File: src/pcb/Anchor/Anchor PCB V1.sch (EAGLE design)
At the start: 8 parts, among them Q1 48 MHz, U1 ATSAMD21G-A

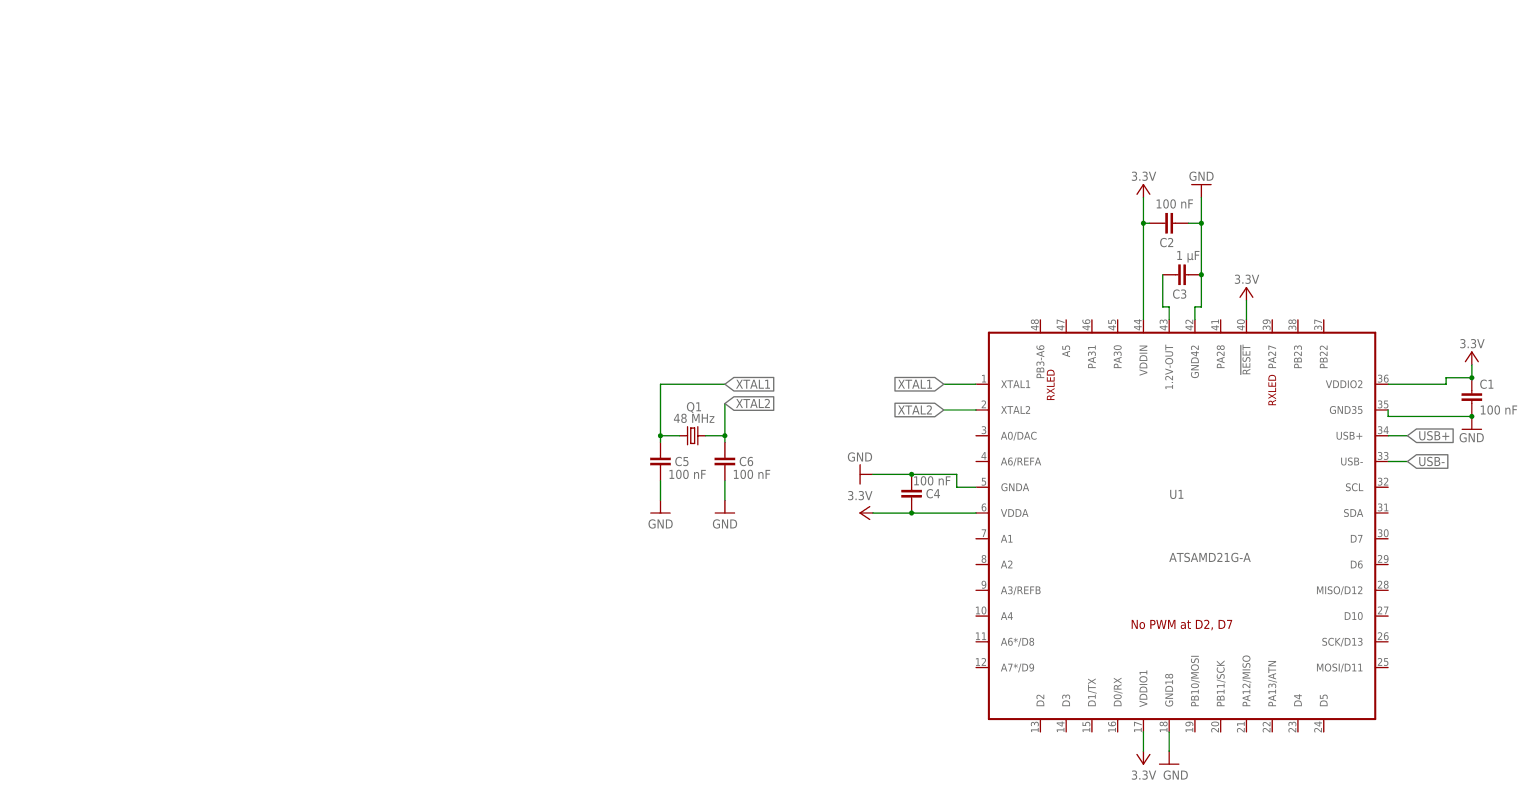
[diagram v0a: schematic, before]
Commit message: Added components
Added DC DC converter
Added reset button
Added mini-USB connection
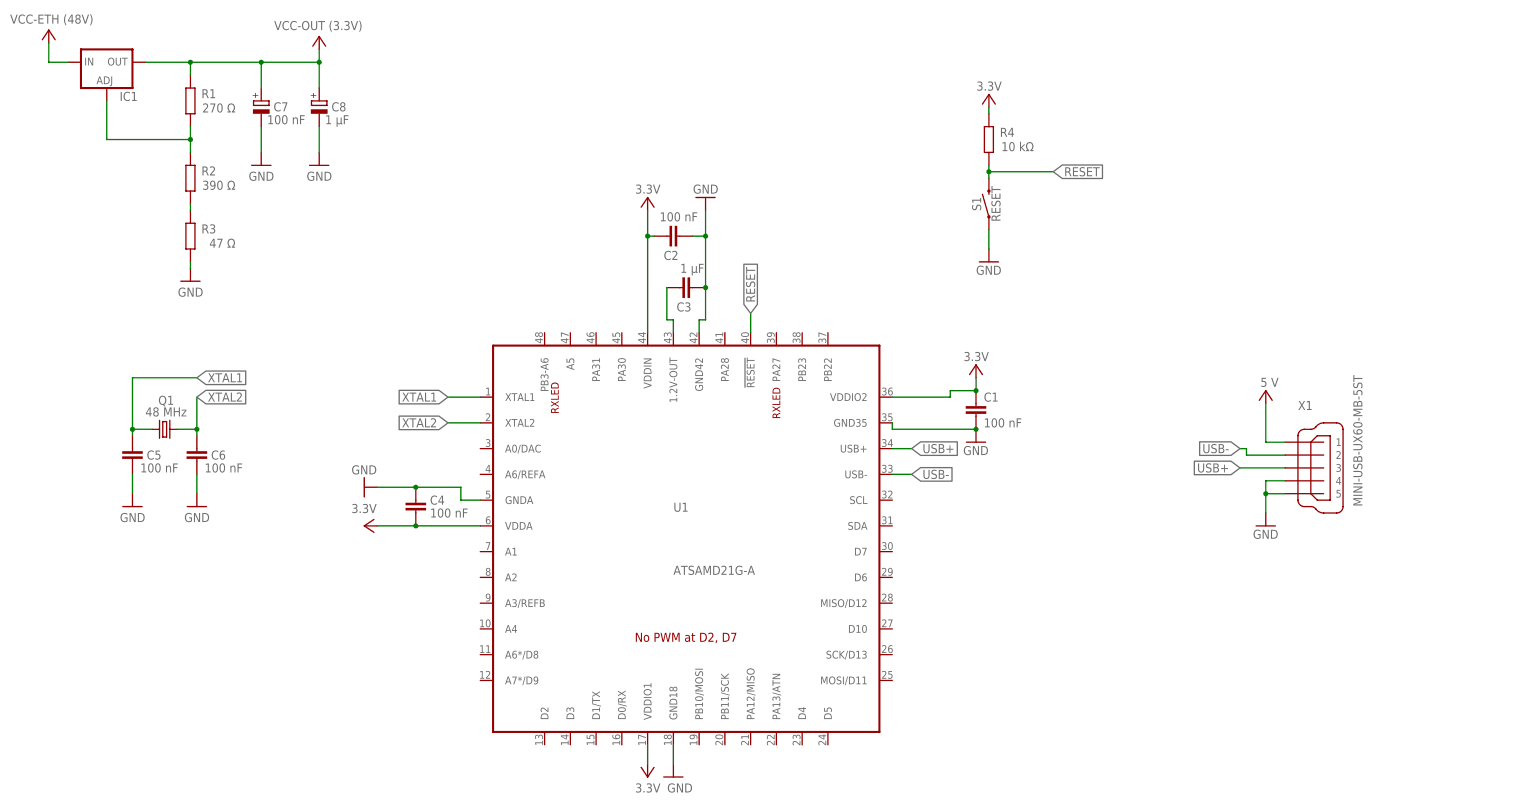
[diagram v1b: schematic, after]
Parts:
- added C7: 100 nF, rcl:CPOL-EUE7.5-18
- added C8: 1 µF, rcl:CPOL-EUE7.5-18
- added IC1: (no value), v-reg:LM317TL
- added R1: 270 Ω, rcl:R-EU_M0805
- added R2: 390 Ω, rcl:R-EU_M0805
- added R3: 47 Ω, rcl:R-EU_M0805
- added R4: 10 kΩ, rcl:R-EU_M0805
- added S1: RESET, SparkFun-Switches:MOMENTARY-SWITCH-SPST-PTH-6.0MM-KIT
- added X1: MINI-USB-UX60-MB-5ST, con-hirose:MINI-USB-UX60-MB-5ST
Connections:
- new net N$4: IC1.ADJ, R1.1, R2.2
- new net N$5: X1.3
- new net N$6: R2.1, R3.2
- new net N$7: X1.2
- new net N$8: R4.1, S1.2
- new net RESET: U1.!RESET!
- net GND: now also C7.-, C8.-, R3.1, S1.1, X1.4, X1.5
- net VCC: now also C7.+, C8.+, IC1.IN, IC1.OUT, R1.2, R4.2, X1.1; no longer U1.!RESET!
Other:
- moved on the sheet: C1, C2, C3, C4, C5, C6, Q1, U1

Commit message: Completed schematic anchor with PoE
PCB design has not been done yet.
Changes might happen in the future
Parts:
- added 10-PIN-PROGRAMMER: (no value), con-lsta:FE05-2
- added BR1, BR2: HD04-T, HD04-T:HD04-T
- added C10: 560 pF, rcl:C-EUC0805
- added C11: 15 pF, rcl:C-EUC0805
- added C12: 33 nF, rcl:C-EUC0805
- added C13: 47 µF (63V), rcl:CPOL-EUB45181D
- added C14, C15: 1 µF (100V), rcl:C-EUC0805
- added C16: 1 µF (16V), rcl:C-EUC0805
- added C17: 0.22 µF (10V), rcl:C-EUC0805
- added C18: 0.1 µF, rcl:C-EUC0805
- added C19, C20, C21: 10 µF (6.3V), rcl:C-EUC0805
- added C22, C24: 10 µF, rcl:CPOL-EUE5-5
- added C23: 100 µF (6.3V), rcl:CPOL-EUUD-5X5,8
- added C25, C26: 100 nF, rcl:C-EUC0805
- added C27: 10 µF, rcl:C-EUC0805
- added C28, C29: 18 µF, rcl:C-EUC0805
- added C9: 0.1 µF (100V), rcl:C-EUC0805
- added D1: SMAJ58A, SMAJ58A:SMAJ58A
- added D2: 6CWQ10FN, shottky:BAS70-05DPAK
- added D3: POWER, SparkFun-LED:LED-BLUE1206
- added D4, D6: TX, SparkFun-LED:LED-YELLOWLILYPAD
- added D5, D7: RX, SparkFun-LED:LED-GREENLILYPAD
- added IC2: TPS23750PWP, TPS23750PWP:TPS23750PWP
- added IC3: REG1117, burr-brown:REG1117
- added IC4: DWM1000, DWM1000:DWM1000
- added J1: 0826-1X1T-GJ-F, 0826-1X1T-GJ-F:0826-1X1T-GJ-F
- added JP1: (no value), jumper:JP1E
- added L1: FB_1206, rc-master-smd:FB_1206
- added L1(74437336100): 10 µH, inductors:DR73
- added L2: 33 µH, inductors:DR73
- added Q2: SUD06N10-225L, transistor-power:N-HEXFET_SOT323-IRLL014N
- added R10: 10 Ω, rcl:R-EU_R0805
- added R11: 1.5 kΩ, rcl:R-EU_R0805
- added R12: 3.48 kΩ, rcl:R-EU_R0805
- added R13: 51.1 Ω, rcl:R-EU_R0805
- added R14, R28: 270 Ω, rcl:R-EU_R0805
- added R15, R16, R17, R18: 49.9 Ω, rcl:R-EU_R0805
- added R19: 2.32 kΩ 1%, rcl:R-EU_R0805
- added R20, R21, R22: 330 Ω, rcl:R-EU_R0805
- added R23: 1 kΩ, rcl:R-EU_R0805
- added R24, R25: 100 Ω, rcl:R-EU_R0805
- added R26, R29: 220 Ω, rcl:R-EU_R0805
- added R27: 10 kΩ, rcl:R-EU_M0805
- added R5: 24,9 kΩ, rcl:R-EU_R0805
- added R6: 100 kΩ, rcl:R-EU_R0805
- added R7: 357 Ω (0.25W), rcl:R-EU_R0805
- added R8: 75 kΩ, rcl:R-EU_R0805
- added R9: 0.18 mΩ (0.5W), rcl:R-EU_R0805
- added Y1: 25 MHz, SparkFun-Clocks:CRYSTALSMD-HC49UP
- C7: device rcl:CPOL-EUE7.5-18 -> rcl:CPOL-EUE5-5
- C8: device rcl:CPOL-EUE7.5-18 -> rcl:CPOL-EUE5-4
- IC1: value (none) -> ENC28J60-I_SS; device v-reg:LM317TL -> ENC28J60-I_SS:ENC28J60-I_SS
- R2: value 390 Ω -> 443 Ω
- R3: value 47 Ω -> 470 Ω; device rcl:R-EU_M0805 -> rcl:R-EU_R0805
- S1: device SparkFun-Switches:MOMENTARY-SWITCH-SPST-PTH-6.0MM-KIT -> SparkFun-Switches:MOMENTARY-SWITCH-SPST-SMD-4.5MM
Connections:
- new net 1_VC+: BR1.~_2, J1.VC12
- new net 1_VC-: BR1.~_1, J1.VC36
- new net 2_VC+: BR2.~_2, J1.VC45
- new net 2_VC-: BR2.~_1, J1.VC78
- new net AUX: C16.1, IC2.AUX
- new net COMP: C11.2, IC2.COMP, R6.2
- new net COM_A_SHTKY: D2.A1, D2.A2, L2.1, Q2.D
- new net CS1: IC1.~CS
- new net CSN_DWM: IC4.SPICSN, U1.D10
- new net FB: C10.1, C11.1, IC2.FB
- new net FREQ: IC2.FREQ, R8.2
- new net GATE: IC2.GATE, R10.1
- new net GRN_CAT: J1.GRN_CAT, R24.1
- new net GRN_LED: IC1.LEDA, J1.GRN_AN
- new net IRQ: IC4.IRQ/GPIO8, R27.2
- new net MISO1_MC: R20.1, U1.PA12/MISO
- new net MISO2_MC: IC4.SPIMISO, U1.MISO/D12
- new net MOSI1_MC: R21.1, U1.PB10/MOSI
- new net MOSI2_MC: IC4.SPIMOSI, U1.MOSI/D11
- new net N$10: R12.1, R13.2
- new net N$11: D4.A, R14.1
- new net N$12: D5.A, R26.1
- new net N$13: D6.A, R28.1
- new net N$14: D7.A, R29.1
- new net N$9: D3.A, R3.1
- new net OSC1: C28.1, IC1.OSC1, Y1.1
- new net OSC2: C29.1, IC1.OSC2, Y1.2
- new net POE+: BR1.+, BR2.+, C13.+, C9.1, D1.K, IC2.VDD, L1(74437336100).1, R5.2
- new net REG_GND: C22.+, IC3.GND, R1.1, R2.2
- new net RSP: IC2.RSP, Q2.S, R9.2
- new net RST_DWM: IC4.RSTN, U1.D6
- new net RTN: C12.2, C13.-, C14.2, C15.2, C16.2, C17.2, IC2.BL, IC2.COM, IC2.MODE, IC2.RSN, IC2.RTN, R8.1, R9.1
- new net RXLED_DWM: D7.C, IC4.GPIO2_/_RXLED
- new net RX_MC: D5.C, U1.D0/RX, U1.PB23
- new net SCK1_MC: R22.1, U1.PB11/SCK
- new net SCK2_MC: IC4.SPICLK, U1.SCK/D13
- new net SCK_ETH: IC1.SCK, R22.2
- new net SEN: C18.1, IC2.SEN, R11.1, R12.2
- new net SI_ETH: IC1.SI, R21.2
- new net SO_ETH: IC1.SO, R20.2
- new net SWCLK: 10-PIN-PROGRAMMER.4, R23.1, U1.PA30
- new net SWDIO: 10-PIN-PROGRAMMER.2, U1.PA31
- new net SWO: 10-PIN-PROGRAMMER.6
- new net TMR: C12.1, IC2.TMR
- new net TPIN+: IC1.TPIN+, J1.TRD2+, R17.1
- new net TPIN-: IC1.TPIN-, J1.TRD2-, R18.2
- new net TPOUT+: IC1.TPOUT+, J1.TRD1+, R15.1
- new net TPOUT-: IC1.TPOUT-, J1.TRD1-, R16.2
- new net TXLED_DWM: D6.C, IC4.GPIO3_/_TXLED
- new net TX_MC: D4.C, U1.D1/TX, U1.PB22
- new net VBIAS: C17.1, IC2.VBIAS
- new net VBUS: X1.1
- new net VCAP: C27.1, IC1.VCAP
- new net VOUT+: C14.1, C15.1, C19.1, C20.1, C21.1, C23.+, C24.+, D2.C, IC2.SENP, IC3.VIN, JP1.1, L1(74437336100).2, R11.2
- new net YEL_CAT: J1.YEL_CAT, R25.1
- new net YEL_LED: IC1.LEDB, J1.YEL_AN
- net GND: now also 10-PIN-PROGRAMMER.3, 10-PIN-PROGRAMMER.5, 10-PIN-PROGRAMMER.9, BR1.-, BR2.-, C18.2, C19.2, C20.2, C21.2, C22.-, C23.-, C24.-, C25.2, C26.2, C27.2, C28.2, C29.2, C9.2, D1.A, D3.C, IC1.VSS, IC1.VSSOSC, IC1.VSSPLL, IC1.VSSRX, IC1.VSSTX, IC2.POWERPAD, IC2.VSS, IC4.VSS_1, IC4.VSS_2, IC4.VSS_3, IC4.VSS_4, IC4.VSS_5, JP1.2, L2.2, R13.1, R19.2, R2.1, R24.2, R25.2, R27.1, R7.1; no longer R3.1
- net N$2: now also IC2.DET, R5.1; no longer C5.1, Q1.2
- net N$3: now also IC2.CLASS, R7.2; no longer C6.1, Q1.1
- net N$4: now also C25.1, J1.TRCT1, L1.1, R15.2, R16.1; no longer IC1.ADJ, R1.1, R2.2
- net N$5: now also C10.2, R6.1; no longer X1.3
- net N$6: now also C26.1, J1.TRCT2, R17.2, R18.1; no longer R2.1, R3.2
- net N$7: now also Q2.G, R10.2; no longer X1.2
- net N$8: now also IC1.RBIAS, R19.1; no longer R4.1, S1.2
- net RESET: now also 10-PIN-PROGRAMMER.10, R4.1, S1.2
- net USB+: now also X1.3
- net USB-: now also X1.2
- net VCC: now also 10-PIN-PROGRAMMER.1, IC1.VDD, IC1.VDDOSC, IC1.VDDPLL, IC1.VDDRX, IC1.VDDTX, IC1.~RESET, IC3.VOUT, IC4.VDD3V3_1, IC4.VDDAON, L1.2, R14.2, R23.2, R26.2, R28.2, R29.2, R3.2; no longer IC1.IN, IC1.OUT, X1.1
- net XTAL1: now also C5.1, Q1.2
- net XTAL2: now also C6.1, Q1.1
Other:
- moved on the sheet: C1, C2, C3, C4, C5, C6, C7, C8, Q1, R1, R2, R3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

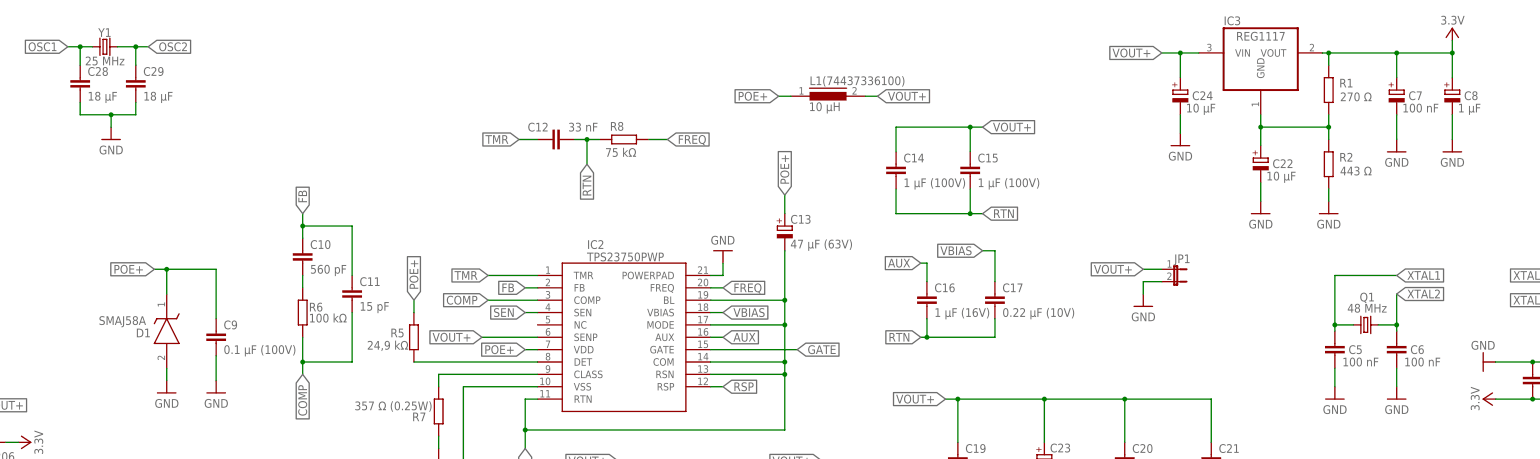
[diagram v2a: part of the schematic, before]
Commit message: Updated capacitor values XTAL
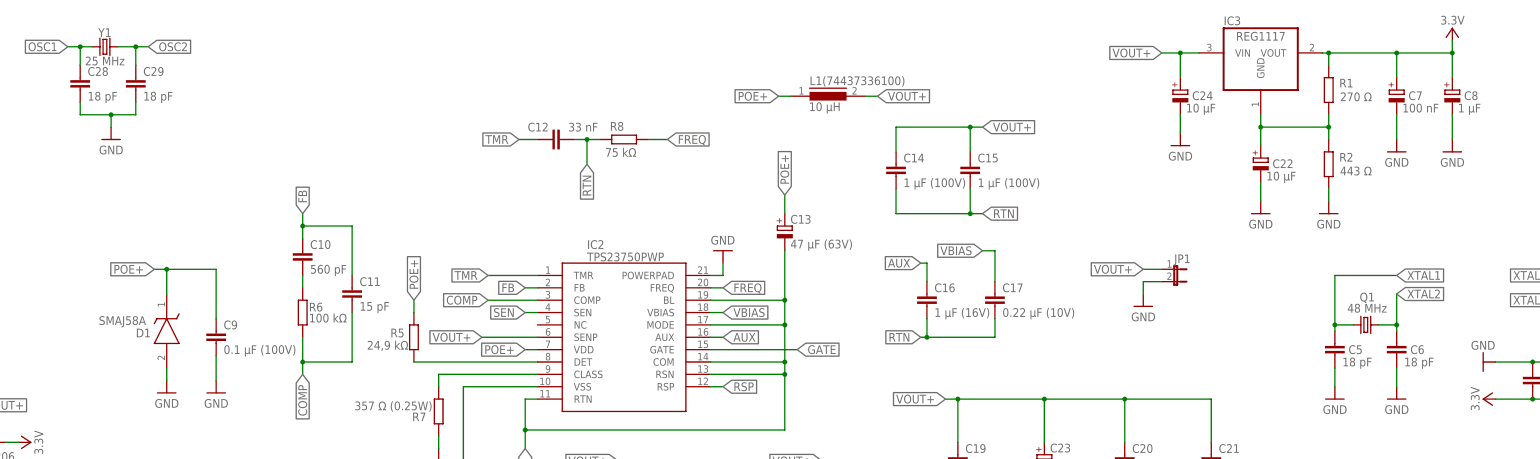
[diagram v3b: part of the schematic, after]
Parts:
- C28, C29: value 18 µF -> 18 pF
- C5, C6: value 100 nF -> 18 pF
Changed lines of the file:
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@@
 <part name="C4" library="rcl" library_urn="urn:adsk.eagle:library:334" deviceset="C-EU" device="C0805" package3d_urn="urn:adsk.eagle:package:23617/2" value="100 nF"/>
 <part name="GND4" library="supply1" library_urn="urn:adsk.eagle:library:371" deviceset="GND" device=""/>
-<part name="C5" library="rcl" library_urn="urn:adsk.eagle:library:334" deviceset="C-EU" device="C0805" package3d_urn="urn:adsk.eagle:package:23617/2" value="100 nF"/>
-<part name="C6" library="rcl" library_urn="urn:adsk.eagle:library:334" deviceset="C-EU" device="C0805" package3d_urn="urn:adsk.eagle:package:23617/2" value="100 nF"/>
+<part name="C5" library="rcl" library_urn="urn:adsk.eagle:library:334" deviceset="C-EU" device="C0805" package3d_urn="urn:adsk.eagle:package:23617/2" value="18 pF"/>
+<part name="C6" library="rcl" library_urn="urn:adsk.eagle:library:334" deviceset="C-EU" device="C0805" package3d_urn="urn:adsk.eagle:package:23617/2" value="18 pF"/>
 <part name="GND5" library="supply1" library_urn="urn:adsk.eagle:library:371" deviceset="GND" device=""/>
 <part name="GND6" library="supply1" library_urn="urn:adsk.eagle:library:371" deviceset="GND" device=""/>
@@
 <part name="P+11" library="supply1" library_urn="urn:adsk.eagle:library:371" deviceset="VCC" device="" value="3.3V"/>
 <part name="GND40" library="supply1" library_urn="urn:adsk.eagle:library:371" deviceset="GND" device=""/>
-<part name="C28" library="rcl" library_urn="urn:adsk.eagle:library:334" deviceset="C-EU" device="C0805" package3d_urn="urn:adsk.eagle:package:23617/2" value="18 µF"/>
-<part name="C29" library="rcl" library_urn="urn:adsk.eagle:library:334" deviceset="C-EU" device="C0805" package3d_urn="urn:adsk.eagle:package:23617/2" value="18 µF"/>
+<part name="C28" library="rcl" library_urn="urn:adsk.eagle:library:334" deviceset="C-EU" device="C0805" package3d_urn="urn:adsk.eagle:package:23617/2" value="18 pF"/>
+<part name="C29" library="rcl" library_urn="urn:adsk.eagle:library:334" deviceset="C-EU" device="C0805" package3d_urn="urn:adsk.eagle:package:23617/2" value="18 pF"/>
 <part name="Y1" library="SparkFun-Clocks" deviceset="CRYSTAL" device="SMD-HC49UP" value="25 MHz"/>
 <part name="P+12" library="supply1" library_urn="urn:adsk.eagle:library:371" deviceset="VCC" device="" value="3.3V"/>

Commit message: First version of PCB layout
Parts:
- removed C22, C24: 10 µF, rcl:CPOL-EUE5-5
- removed C7: 100 nF, rcl:CPOL-EUE5-5
- removed C8: 1 µF, rcl:CPOL-EUE5-4
- removed IC3: REG1117, burr-brown:REG1117
- removed R1: 270 Ω, rcl:R-EU_M0805
- removed R2: 443 Ω, rcl:R-EU_M0805
- added C30: 22 µF, rcl:CPOL-EUE5-5
- added C31: 0.1 µF, rcl:CPOL-EUE5-4
- added D8: 1PS79SB10, nxp_60_1_1:1PS79SB10
- added D9: PRTR5V0U2X,215, PRTR5V0U2X_215:PRTR5V0U2X,215
- added IC5: MIC5209-3.3YS-TR, MIC5209-3.3YS-TR:MIC5209-3.3YS-TR
- added JP2, JP3: (no value), jumper:JP1E
- C13: device rcl:CPOL-EUB45181D -> rcl:CPOL-EUE3.5-8
- Q1: value 48 MHz -> 32 MHz
- R9: device rcl:R-EU_R0805 -> rcl:R-EU_R2010
- X1: value MINI-USB-UX60-MB-5ST -> MICRO-USB-RECEPTACLE47589-0001; device con-hirose:MINI-USB-UX60-MB-5ST -> con-molex-usb:MICRO-USB-RECEPTACLE47589-0001
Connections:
- removed net REG_GND: C22.+, IC3.GND, R1.1, R2.2
- new net ID: X1.4
- new net N$15: D8.K, D9.VCC
- net GND: now also C30.-, C31.-, D9.GND, IC5.GND, IC5.GND_(TAB), JP2.2, JP3.2, X1.GND1, X1.GND2, X1.GND3, X1.GND4; no longer C22.-, C24.-, C7.-, C8.-, R2.1, X1.4
- net POE+: now also JP3.1
- net USB+: now also D9.I/O_1
- net USB-: now also D9.I/O_2
- net VBUS: now also D8.A
- net VCC: now also C30.+, IC5.OUT, JP2.1; no longer C7.+, C8.+, IC3.VOUT, R1.2
- net VOUT+: now also C31.+, IC5.IN; no longer C24.+, IC3.VIN
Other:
- moved on the sheet: 10-PIN-PROGRAMMER, BR1, BR2, C1, C12, C14, C15, C16, C17, C2, C25, C26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

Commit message: Updating board
Update board so that we are using parts that are available in the labo.
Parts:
- removed BR1, BR2: HD04-T, HD04-T:HD04-T
- removed C30: 22 µF, rcl:CPOL-EUE5-5
- removed C31: 0.1 µF, rcl:CPOL-EUE5-4
- removed IC5: MIC5209-3.3YS-TR, MIC5209-3.3YS-TR:MIC5209-3.3YS-TR
- removed X1: MICRO-USB-RECEPTACLE47589-0001, con-molex-usb:MICRO-USB-RECEPTACLE47589-0001
- added B1, B2: DBS103G, rectifier:DBS103G
- added C22: 470 pF, rcl:C-EUC0805
- added C24: 2.2 µF, rcl:C-EUC0805
- added C7: 100 nF, rcl:C-EUC0805
- added C8: 1 µF, rcl:C-EUC0805
- added IC3: MIC5219-3.3YM5-TR, MIC5219-3.3YM5-TR:MIC5219-3.3YM5-TR
- added J2: 105017-0001, 105017-0001:105017-0001
- Q1: device crystal:CRYSTALCTS406 -> abracon:CRYSTAL.ABS07
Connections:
- removed net POE+: BR1.+, BR2.+, C13.+, C9.1, D1.K, IC2.VDD, JP3.1, L1(74437336100).1, R5.2
- removed net VOUT+: C14.1, C15.1, C19.1, C20.1, C21.1, C23.+, C31.+, D2.C, IC2.SENP, IC5.IN, JP1.1, L1(74437336100).2, R11.2
- new net 48V: B1.+, B2.+, C13.+, C9.1, D1.K, IC2.VDD, JP3.1, L1(74437336100).1, R5.2
- new net 5V: C14.1, C15.1, C19.1, C20.1, C21.1, C23.+, D2.C, IC2.SENP, IC3.EN, IC3.IN, JP1.1, L1(74437336100).2, R11.2
- new net N$18: C22.2, IC3.BYP
- net 1_VC+: now also B2.AC1; no longer BR1.~_2
- net 1_VC-: now also B2.AC2; no longer BR1.~_1
- net 2_VC+: now also B1.AC2; no longer BR2.~_2
- net 2_VC-: now also B1.AC1; no longer BR2.~_1
- net GND: now also B1.-, B2.-, C22.1, C24.2, C7.1, C8.1, IC3.GND, J2.GND; no longer BR1.-, BR2.-, C30.-, C31.-, IC5.GND, IC5.GND_(TAB), X1.5, X1.GND1, X1.GND2, X1.GND3, X1.GND4
- net ID: now also J2.ID; no longer X1.4
- net USB+: now also J2.D+; no longer X1.3
- net USB-: now also J2.D-; no longer X1.2
- net VBUS: now also J2.VDD; no longer X1.1
- net VCC: now also C24.1, C7.2, C8.2, IC3.OUT; no longer C30.+, IC5.OUT
